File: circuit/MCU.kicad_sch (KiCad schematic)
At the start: 47 parts, among them J1 SH_01x07, J19 USB_C_Receptacle_USB2.0_14P, Q1 DMP1011UCB9-7, Q2 DMN1054UCB4, Q3 DMN1054UCB4, SW1 SW_Push, U1 R5F5671EHGLE, U2 NSVT3906DXV6T1G, X1 OT322516MJBA4SL, X2 X1A0000610006

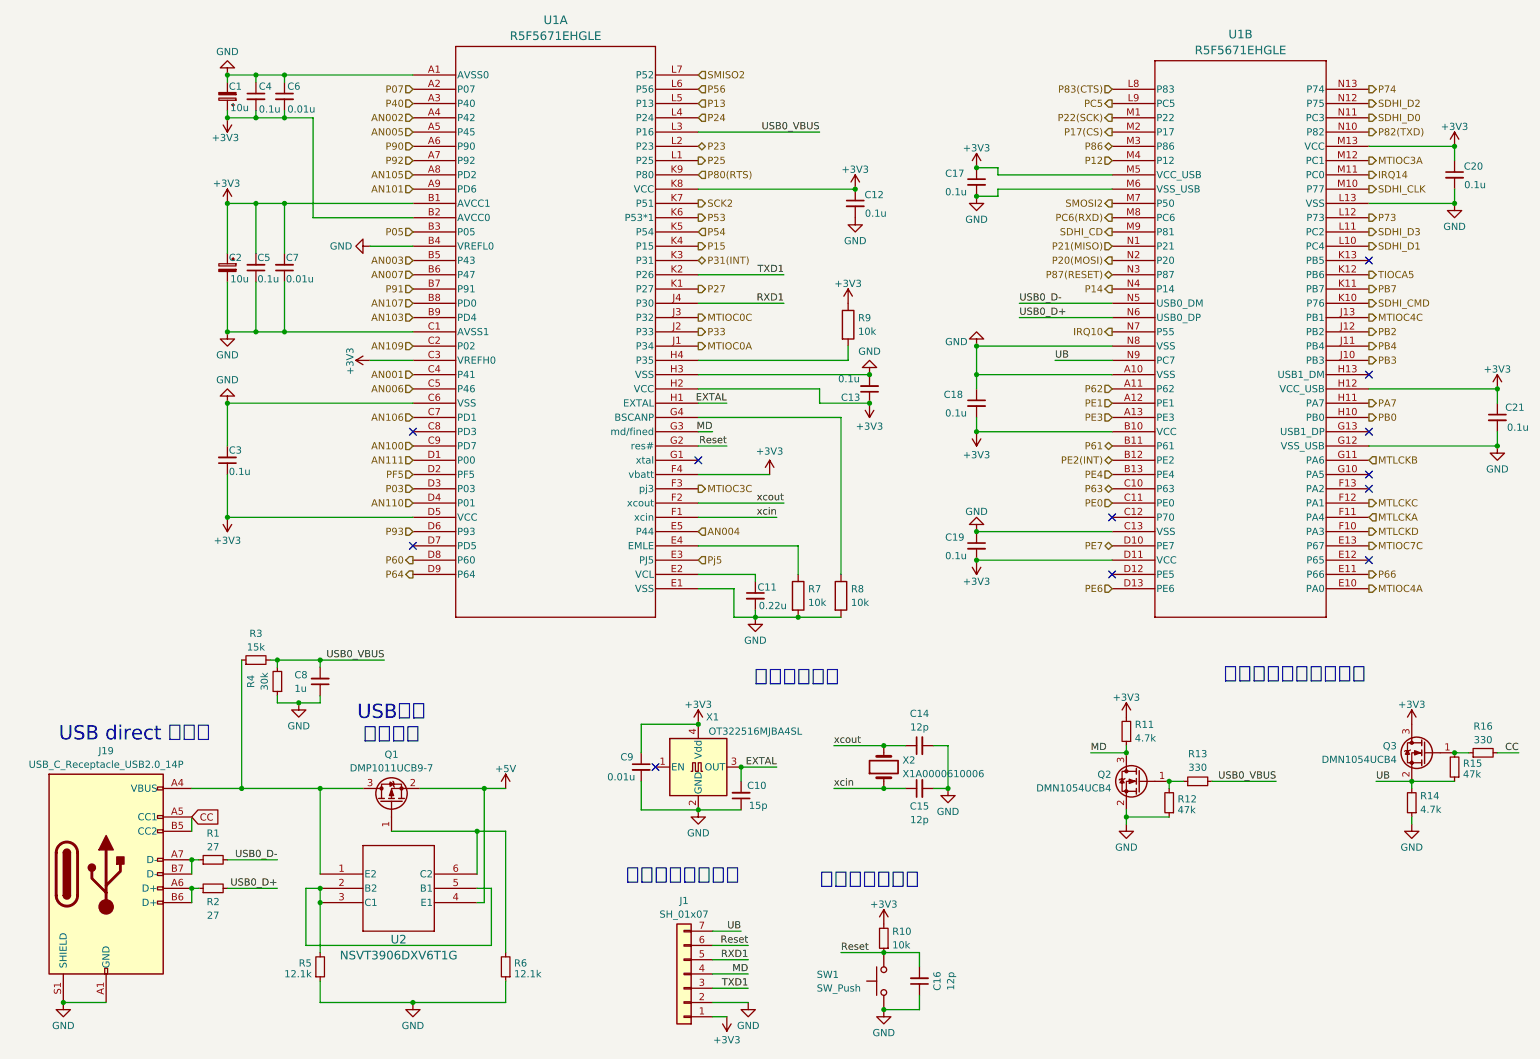
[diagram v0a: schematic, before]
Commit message: スマコンの設定変更 回路図変更
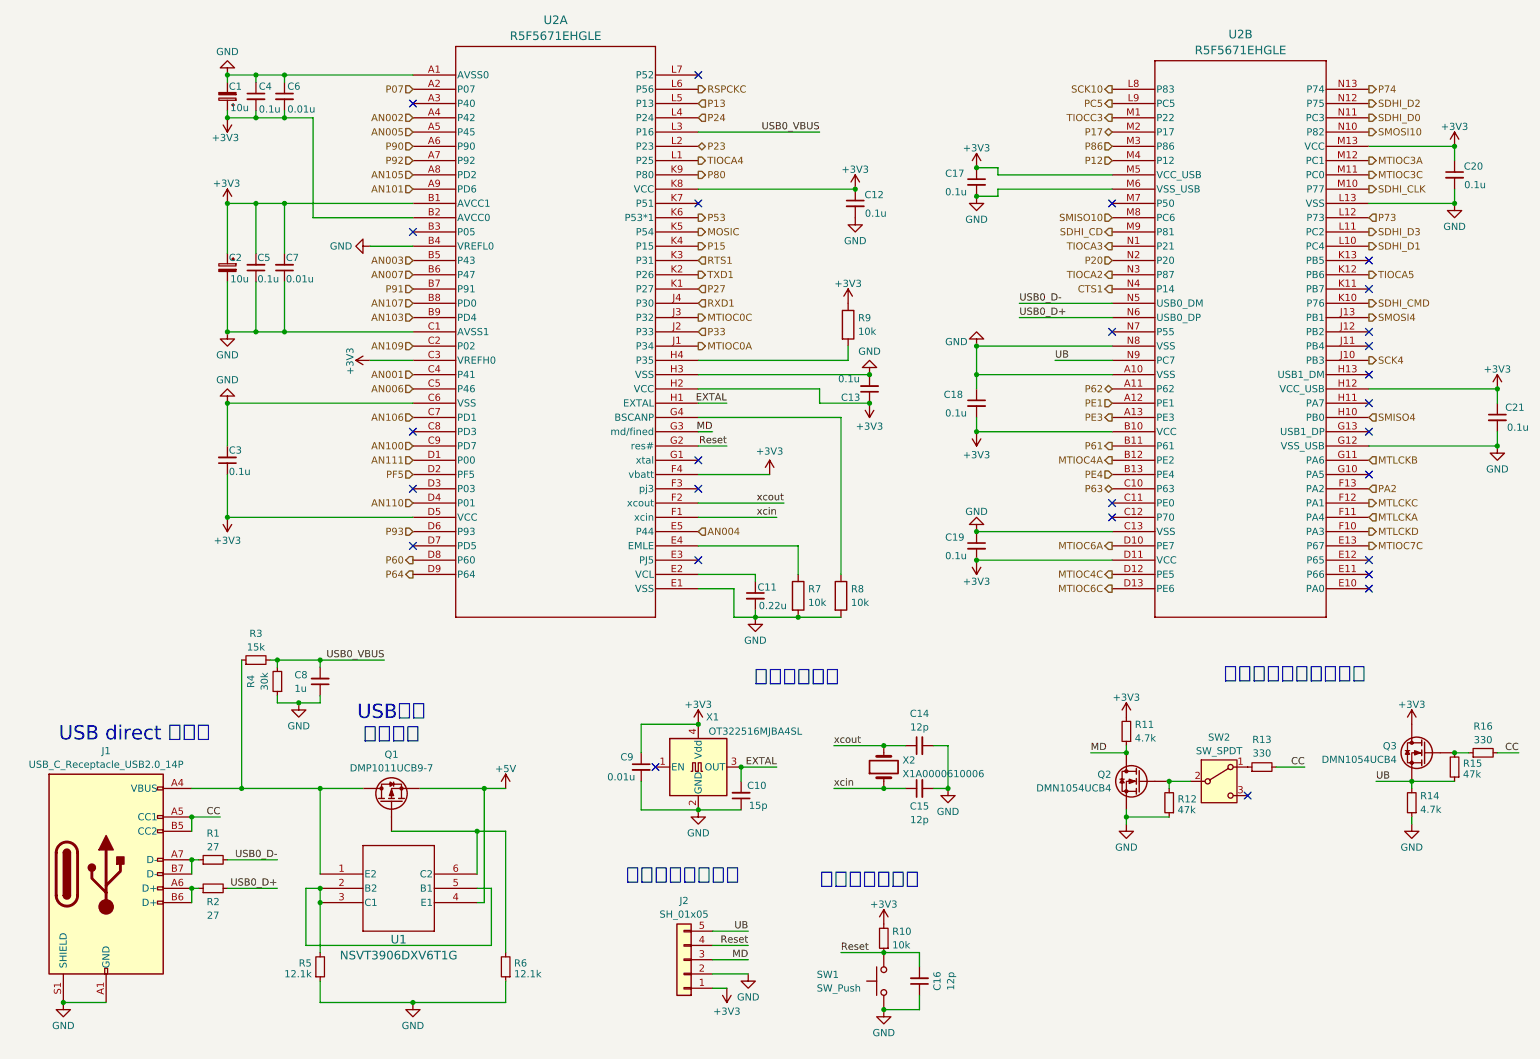
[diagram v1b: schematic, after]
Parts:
- removed J1: SH_01x07, Connector_JST:JST_SH_BM07B-SRSS-TB_1x07-1MP_P1.00mm_Vertical, symbol Connector_Generic:Conn_01x07
- added J2: SH_01x05, symbol Connector_Generic:Conn_01x05
- added SW2: SW_SPDT, symbol Switch:SW_SPDT
- Q1: symbol Device:Q_PMOS_GSD -> Device:Q_PMOS
- Q2, Q3: symbol Device:Q_NMOS_GSD -> Device:Q_NMOS
- U1: renamed from U2; symbol robocon:NSVT3906DXV6T1G -> robot_contest:NSVT3906DXV6T1G
- U2: renamed from U1; symbol robocon:R5F5671EHGLE-20 -> robot_contest:R5F5671EHGLE-20
- renumbered J19 to J1
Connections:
- net IRQ14 is gone; now on net MTIOC3C: U2.M11 (PC0)
- net PE2(INT) is gone; now on net MTIOC4A: U2.B12 (PE2)
- net +3V3: now also Q3.D, J2.1 (Pin_1); no longer Q3.3 (D)
- net +5V: now also Q1.S; no longer Q1.2 (S)
- net CC: now also R13.2
- net GND: now also Q2.S, J2.2 (Pin_2); no longer Q2.2 (S)
- net MD: now also Q2.D, J2.3 (Pin_3); no longer Q2.3 (D)
- net MTIOC3C: no longer U2.F3 (pj3)
- net MTIOC4A: no longer U2.E10 (PA0)
- net MTIOC4C: now also U2.D12 (PE5); no longer U2.J13 (PB1)
- net Reset: now also J2.4 (Pin_4)
- net UB: now also Q3.S, J2.5 (Pin_5); no longer Q3.2 (S)
- net USB0_VBUS: no longer R13.2
- net at R15.2, R16.1: now also Q3.G; no longer Q3.1 (G)
- net at R6.2, U1.6 (C2): now also Q1.G; no longer Q1.1 (G)
- net at J1.A4 (VBUS), J1.A9 (VBUS), J1.B4 (VBUS)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: now also Q1.D; no longer Q1.3 (D)
- net PA2: now reaches U2.F13 (PA2)
- net IRQ10: no longer names the net of U2.N7 (P55)
- net P03: no longer names the net of U2.D3 (P03)
- net P05: no longer names the net of U2.B3 (P05)
- net P14 renamed CTS1
- net P17(CS) renamed P17
- net P20(MOSI) renamed P20
- net P21(MISO) renamed TIOCA3
- net P22(SCK) renamed TIOCC3
- net P25 renamed TIOCA4
- net P31(INT) renamed RTS1
- net P40: no longer names the net of U2.A3 (P40)
- net P54 renamed MOSIC
- net P56 renamed RSPCKC
- net P66: no longer names the net of U2.E11 (P66)
- net P80(RTS) renamed P80
- net P82(TXD) renamed SMOSI10
- net P83(CTS) renamed SCK10
- net P87(RESET) renamed TIOCA2
- net PA7: no longer names the net of U2.H11 (PA7)
- net PB0 renamed SMISO4
- net PB2: no longer names the net of U2.J12 (PB2)
- net PB3 renamed SCK4
- net PB4: no longer names the net of U2.J11 (PB4)
- net PB7: no longer names the net of U2.K11 (PB7)
- net PC6(RXD) renamed SMISO10
- net PE0: no longer names the net of U2.C11 (PE0)
- net PE6 renamed MTIOC6C
- net PE7 renamed MTIOC6A
- net Pj5: no longer names the net of U2.E3 (PJ5)
- net SCK2: no longer names the net of U2.K7 (P51)
- net SMISO2: no longer names the net of U2.L7 (P52)
- net SMOSI2: no longer names the net of U2.M7 (P50)
- new net: R13.1, SW2.1 (A)
- new net: Q2.G, R12.2, SW2.2 (B)
- new net SMOSI4: U2.J13 (PB1)
- no-connect marks 12 -> 27
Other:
- moved on the sheet: R13
